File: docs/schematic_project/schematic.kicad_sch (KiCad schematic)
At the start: 2 parts, among them J1 Raspberry_Pi_5, U1 28C256

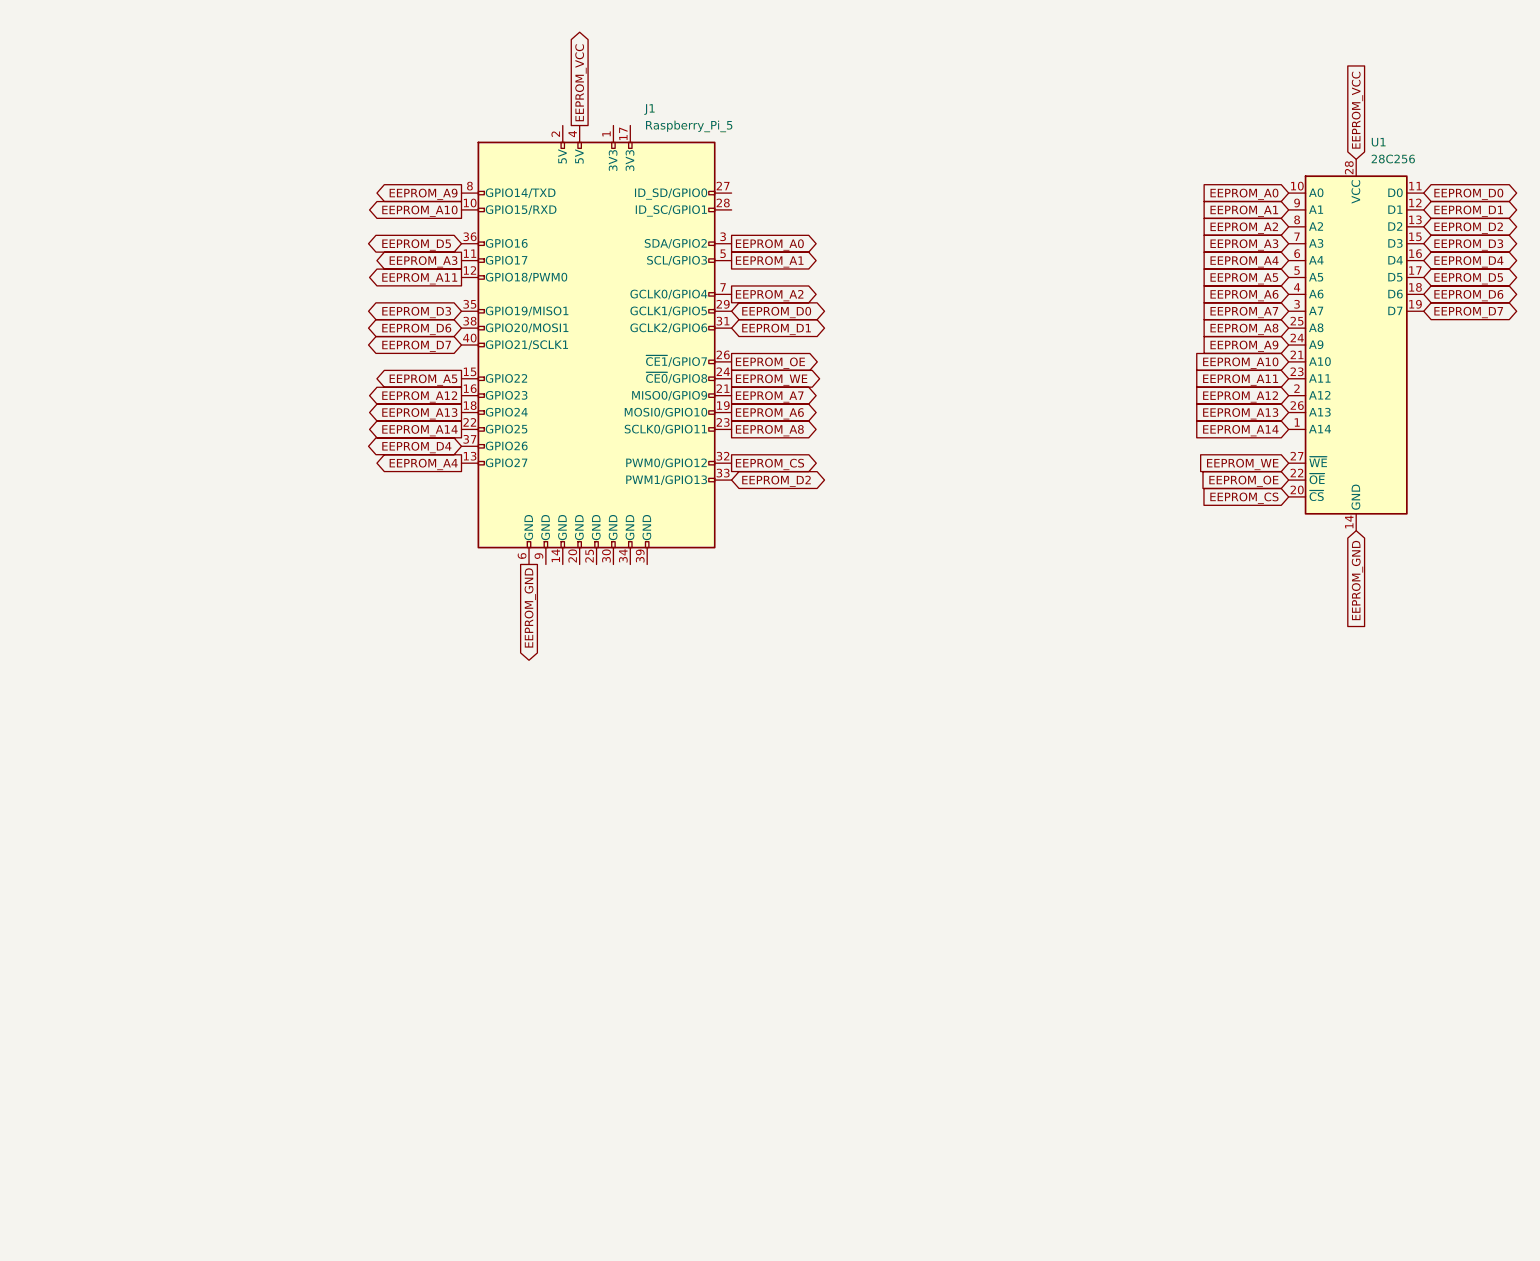
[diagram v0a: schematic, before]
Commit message: Export schematic to SVG
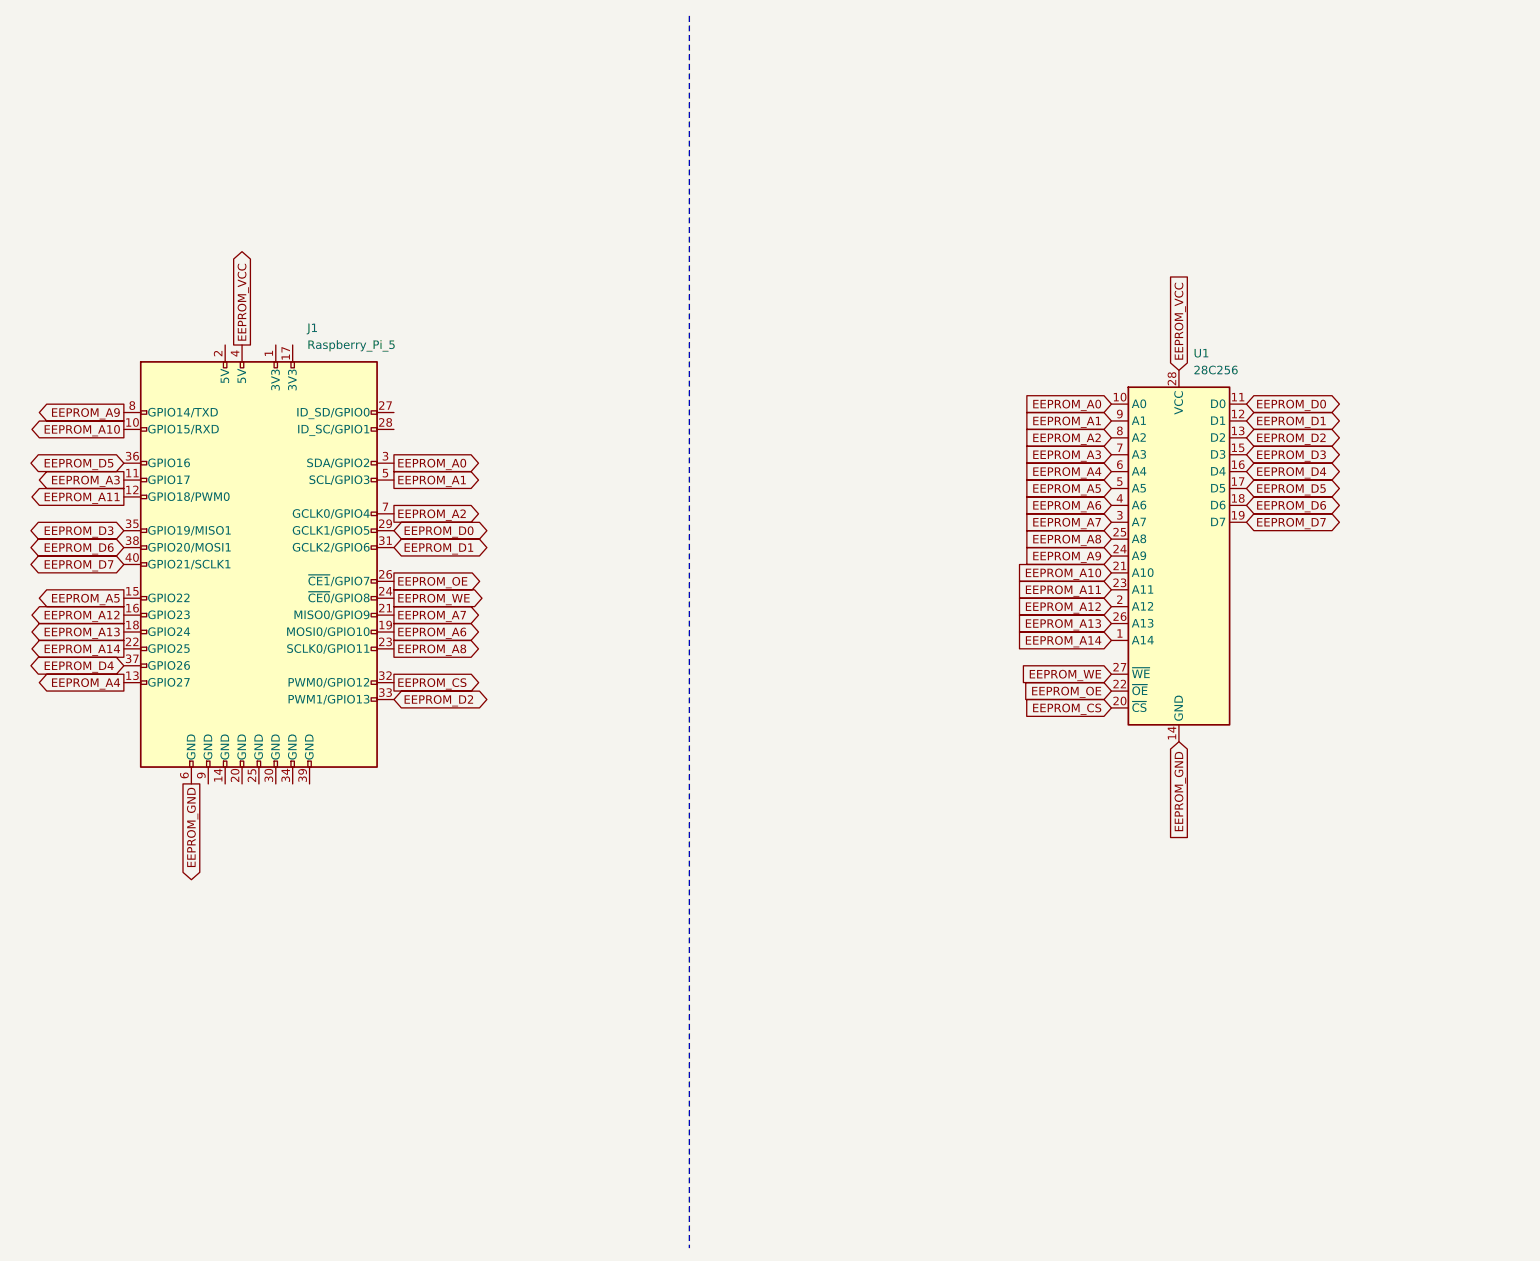
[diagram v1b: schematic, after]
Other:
- company: (none) -> Joel Sanz Martí
- title: (none) -> EEPROM Manager
- moved on the sheet: J1, U1
